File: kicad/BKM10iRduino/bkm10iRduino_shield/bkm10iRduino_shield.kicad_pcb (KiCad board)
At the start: 4 copper layers, 20.3 x 80 mm, 6 parts, among them J1 RJ45, SW1 SW_SPST, U1 TSOP343xx, U2 MAX485E

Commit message: update pcb
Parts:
- moved U2 20.9 mm to (171.4, 110.5), turned to 90 degrees
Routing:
- net Net-(J1-Pad2): track 9.99 -> 14.7 mm
- net Net-(J1-Pad7): track 9.91 -> 14.5 mm
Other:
- board text removed: "GND"
- board text removed: "VCC"

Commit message: updated pcb design
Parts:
- removed Brd1: SSD1306, SSD1306:128x64OLED
- added C1: C_Small, Capacitor_SMD:CP_Elec_3x5.3, F.Cu at (174.0, 120.7)
- added D3: D_Small_ALT, Diode_SMD:D_1206_3216Metric_Pad1.42x1.75mm_HandSolder, F.Cu at (165.1, 120.9)
- added D4: D_Small_ALT, Diode_SMD:D_1206_3216Metric_Pad1.42x1.75mm_HandSolder, F.Cu at (170.2, 120.9)
- added D5: SH1106, Connector_PinHeader_2.54mm:PinHeader_1x07_P2.54mm_Vertical, F.Cu at (153.7, 78.7)
- added R1: R, Resistor_SMD:R_1206_3216Metric_Pad1.30x1.75mm_HandSolder, F.Cu at (167.6, 115.6)
- added REF**: MountingHole_2.2mm_M2, MountingHole:MountingHole_2.2mm_M2, F.Cu at (180.3, 121.9)
- added REF**: MountingHole_2.2mm_M2, MountingHole:MountingHole_2.2mm_M2, F.Cu at (153.7, 121.9)
- added REF**: MountingHole_2.2mm_M2, MountingHole:MountingHole_2.2mm_M2, F.Cu at (180.3, 53.3)
- added REF**: MountingHole_2.2mm_M2, MountingHole:MountingHole_2.2mm_M2, F.Cu at (153.7, 53.3)
- A1: footprint Module:Arduino_Nano -> bkm10rduino:Arduino_Nano
- J1: value RJ45 -> DB9_Male; footprint Connector_RJ:RJ45_Amphenol_54602-x08_Horizontal -> Connector_Dsub:DSUB-9_Male_Horizontal_P2.77x2.84mm_EdgePinOffset4.94mm_Housed_MountingHolesOffset7.48mm
- moved J1 9.25 mm to (161.3, 128.3)
- moved SW1 6.35 mm to (175.3, 52.1), turned to 270 degrees
- moved U2 2.54 mm to (171.4, 108.0)
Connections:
- net Net-(J1-Pad2) renamed AB+
- net Net-(J1-Pad7) renamed AB-
- net ~LEARN_BUTTON_IN renamed LEARN_BUTTON_IN
- A1 pad 11: Net-(A1-Pad11) -> RES
- A1 pad 12: Net-(A1-Pad12) -> CS
- A1 pad 13: Net-(A1-Pad13) -> DC
- A1 pad 14: Net-(A1-Pad14) -> MOSI
- A1 pad 16: Net-(A1-Pad16) -> SCK
- A1 pad 2: Net-(A1-Pad2) -> RS485_RX
- A1 pad 6: Net-(A1-Pad6) -> RS485_RX_ENABLE
- J1 pad 3: Net-(J1-Pad3) -> YZ+
- J1 pad 8: Net-(J1-Pad8) -> YZ-
- U2 pad 1: Net-(U2-Pad1) -> RS485_RX
- U2 pad 2: Net-(U2-Pad2) -> RS485_RX_ENABLE
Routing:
- net RS485_RX: track 0.00 -> 51.1 mm
- net SCK: track 0.00 -> 31.9 mm, vias 0 -> 2
- net RS485_RX_ENABLE: track 0.00 -> 30.5 mm, vias 0 -> 2
- net Net-(A1-Pad24): track 28.8 -> 0.00 mm
- net Net-(A1-Pad23): track 26.1 -> 0.00 mm
- net RES: track 0.00 -> 14.8 mm
- net IR_OUT: track 28.4 -> 43.1 mm
- net AB-: track 14.5 -> 27.0 mm
- net YZ-: track 0.00 -> 9.57 mm
- net AB+: track 14.7 -> 23.2 mm
- net DC: track 0.00 -> 7.40 mm
- net CS: track 0.00 -> 7.40 mm
- net YZ+: track 0.00 -> 6.63 mm
- net MOSI: track 0.00 -> 6.35 mm
- net RS485_TX: track 37.1 -> 40.9 mm
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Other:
- board size 20.3 x 80 mm -> 34.3 x 86.4 mm
- board text added: "Arduino Nano"
- board text added: "BKM-10iRduino (2021) aaron@bonham.com.au"
- board text added: "CK"
- board text added: "CS"
- board text added: "DC"
- board text added: "GND"
- board text added: "MOSI"
- board text added: "RES"
- board text added: "VCC"
- board text removed: "A"
- board text removed: "B"

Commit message: pcb redesign
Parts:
- removed D3, D4: D_Small_ALT, Diode_SMD:D_1206_3216Metric_Pad1.42x1.75mm_HandSolder
- removed REF** (x4): MountingHole_2.2mm_M2, MountingHole:MountingHole_2.2mm_M2
- removed U2: MAX485E, bkm10rduino:TLL_RS485
- added C2: C_Small, Capacitor_SMD:C_1812_4532Metric_Pad1.57x3.40mm_HandSolder, F.Cu at (154.9, 104.1)
- added C3: C_Small, Capacitor_SMD:C_1812_4532Metric_Pad1.57x3.40mm_HandSolder, F.Cu at (154.9, 61.0)
- added C4: C_Small, Capacitor_SMD:C_1812_4532Metric_Pad1.57x3.40mm_HandSolder, F.Cu at (170.2, 94.0)
- added IC1: MAX22508EASA+, SamacSys_Parts:SOP50P490X110-10N, F.Cu at (167.6, 100.3)
- A1: footprint bkm10rduino:Arduino_Nano -> Module:Arduino_Nano
- C1: footprint Capacitor_SMD:CP_Elec_3x5.3 -> Capacitor_SMD:C_1812_4532Metric_Pad1.57x3.40mm_HandSolder
- J1: footprint Connector_Dsub:DSUB-9_Male_Horizontal_P2.77x2.84mm_EdgePinOffset4.94mm_Housed_MountingHolesOffset7.48mm -> Connector_Dsub:DSUB-9_Male_Vertical_P2.77x2.84mm_MountingHoles; moved to B.Cu
- moved C1 17.7 mm to (180.3, 104.1)
- moved J1 11.4 mm to (161.3, 116.8)
- moved R1 8.89 mm to (167.9, 106.7)
- moved D5 8.89 mm to (153.7, 69.8), turned to 0 degrees
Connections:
- A1 pad 5: RS485_TX_ENABLE -> RS485_RX_ENABLE
- A1 pad 6: RS485_RX_ENABLE -> RS485_TX_ENABLE
- J1 pad 2: AB+ -> AB-
- J1 pad 7: AB- -> AB+
- R1 pad 1: AB+ -> YZ+
- R1 pad 2: AB- -> YZ-
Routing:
- net RS485_RX: track 51.1 -> 6.37 mm
- net RS485_TX: track 40.9 -> 6.81 mm
- net GND: track 2.31 -> 24.2 mm, vias 1 -> 4
- net RS485_RX_ENABLE: track 30.5 -> 10.4 mm, vias 2 -> 0
- net RS485_TX_ENABLE: track 32.6 -> 13.0 mm, vias 2 -> 0
- net IR_OUT: track 43.1 -> 28.4 mm
- net YZ+: track 6.63 -> 17.5 mm
- net VCC: track 2.31 -> 11.8 mm, vias 1 -> 4
- net MOSI: track 6.35 -> 13.9 mm
- net YZ-: track 9.57 -> 15.2 mm
- net CS: track 7.40 -> 12.5 mm
- net SCK: track 31.9 -> 26.8 mm, vias 2 -> 0
- net AB+: track 23.2 -> 18.8 mm, vias 0 -> 1
- net AB-: track 27.0 -> 23.2 mm, vias 0 -> 1
- net RES: track 14.8 -> 11.4 mm
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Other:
- board size 34.3 x 86.4 mm -> 34.3 x 73.7 mm

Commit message: more updates to board
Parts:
- added REF**: MountingHole_3.2mm_M3, MountingHole:MountingHole_3.2mm_M3, F.Cu at (153.7, 53.3)
- added REF**: MountingHole_3.2mm_M3, MountingHole:MountingHole_3.2mm_M3, F.Cu at (180.3, 53.3)
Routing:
- added copper zone on B.Cu, net (none)
- added copper zone on F.Cu, net (none)

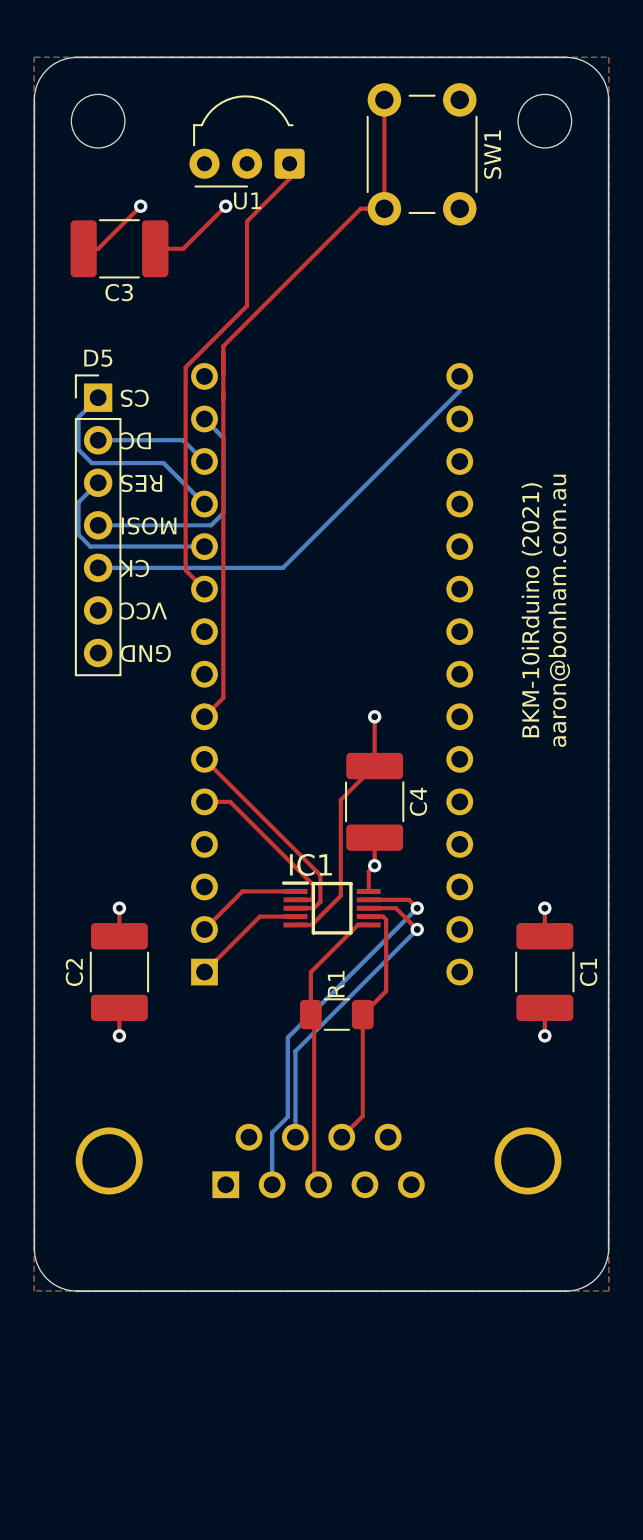
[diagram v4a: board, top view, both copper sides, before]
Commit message: many fixes to pcb layout, use full duplex RS485
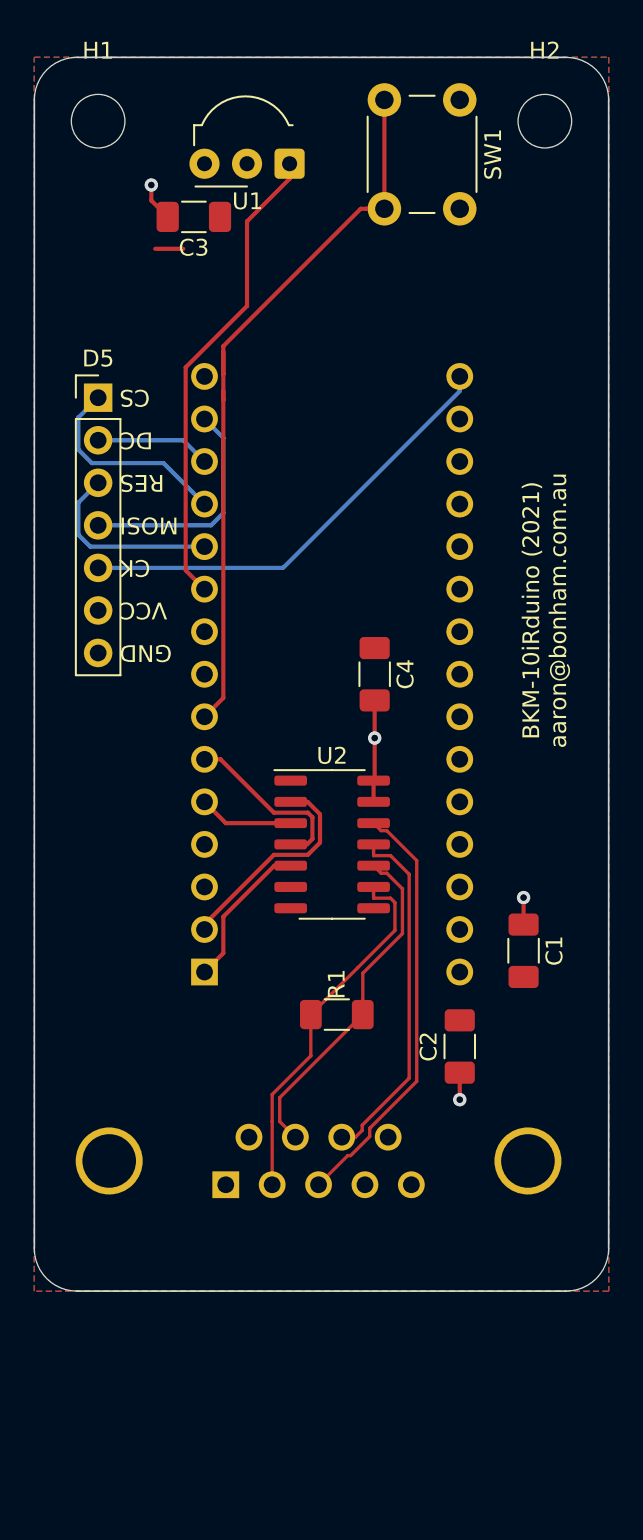
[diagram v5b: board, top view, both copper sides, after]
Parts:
- removed IC1: MAX22508EASA+, SamacSys_Parts:SOP50P490X110-10N
- removed REF** (x2): MountingHole_3.2mm_M3, MountingHole:MountingHole_3.2mm_M3
- added H1: MountingHole, MountingHole:MountingHole_3.2mm_M3, F.Cu at (153.7, 53.3)
- added H2: MountingHole, MountingHole:MountingHole_3.2mm_M3, F.Cu at (180.3, 53.3)
- added U2: ADM3063EARZ-ND, Package_SO:SOIC-14_3.9x8.7mm_P1.27mm, F.Cu at (167.6, 96.5)
- C1, C2, C3, C4: footprint Capacitor_SMD:C_1812_4532Metric_Pad1.57x3.40mm_HandSolder -> Capacitor_SMD:C_1206_3216Metric_Pad1.33x1.80mm_HandSolder
- moved C2 20.8 mm to (175.3, 108.6)
- moved C4 7.62 mm to (170.2, 86.4)
- moved C3 4.84 mm to (159.4, 59.1)
- moved C1 1.80 mm to (179.1, 102.9)
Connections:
- J1 pad 2: AB- -> YZ+
- J1 pad 3: YZ+ -> AB-
- J1 pad 7: AB+ -> YZ-
- J1 pad 8: YZ- -> AB+
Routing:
- net GND: track 24.2 -> 1.67 mm, vias 4 -> 0
- net RS485_RX: track 6.37 -> 13.0 mm
- net YZ-: track 15.2 -> 20.5 mm
- net RS485_RX_ENABLE: track 10.4 -> 5.67 mm
- net YZ+: track 17.5 -> 21.9 mm
- net RS485_TX_ENABLE: track 13.0 -> 10.6 mm
- net AB+: track 18.8 -> 21.1 mm, vias 1 -> 0
- net RS485_TX: track 6.81 -> 9.05 mm
- net AB-: track 23.2 -> 25.4 mm, vias 1 -> 0
- net VCC: track 11.8 -> 11.0 mm
- added copper zone on F.Cu, net GND
- added copper zone on B.Cu, net VCC
- removed copper zone on B.Cu, net (none)
- removed copper zone on F.Cu, net (none)
- removed copper zone on In2.Cu.Ground, net GND
- removed copper zone on In1.Cu.Power, net VCC
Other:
- copper layers 4 -> 2

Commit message: add 2 layer PBC and also a RP2040 version
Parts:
- moved C1 26.3 mm to (153.7, 95.9), turned to 180 degrees
- moved D5 6.35 mm to (153.7, 76.2)
- moved R1 2.46 mm to (166.4, 104.8), turned to 90 degrees
- moved C4 1.61 mm to (170.2, 88.0)
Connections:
- J1 pad 2: YZ+ -> YZ-
- J1 pad 3: AB- -> AB+
- J1 pad 7: YZ- -> YZ+
- J1 pad 8: AB+ -> AB-
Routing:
- net YZ-: track 20.5 -> 26.0 mm
- net MOSI: track 13.9 -> 18.4 mm
- net RES: track 11.4 -> 7.40 mm
- net AB+: track 21.1 -> 24.6 mm
- net SCK: track 26.8 -> 30.2 mm
- net YZ+: track 21.9 -> 19.0 mm
- net VCC: track 11.0 -> 9.37 mm
- net DC: track 6.88 -> 8.45 mm
- net AB-: track 25.4 -> 24.2 mm
